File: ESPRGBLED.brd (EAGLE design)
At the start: 160 x 100 mm, 20 parts

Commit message: added layout
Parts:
- removed D4: (no value), diode:SMB
- removed PWR1:R3, PWR2:R3, PWR3:R3: 10k, rcl:R0603
- removed PWR1:R4, PWR2:R4, PWR3:R4: (no value), rcl:R0603
- removed PWR1:T2, PWR2:T2, PWR3:T2: (no value), transistor:SOT23-BEC
- removed SV1: (no value), con-lstb:MA03-1
- added C1, C2: (no value), rcl:C0603K
- added C3, C4: (no value), rcl:C0805K
- added D1: MBRS130LT3, diode:SMB
- added U$3: (no value), Fabian:3-WIRE_CONN
- added U$4, U$5, U$6, U$7, U$8: CON1, Fabian:CON1HP
- PWR1:D1, PWR2:D1, PWR3:D1: value (none) -> MBRS130LT3
- PWR1:T1, PWR2:T1, PWR3:T1: value MOSFET-NIRLR8743 -> (none); device Fabian:DPAK -> zetex:SOT223
- moved U$1 26.7 mm to (128.3, 64.8)
- moved R5 21.9 mm to (127.0, 40.6), turned to 180 degrees
- moved PWR1:D1 19.0 mm to (128.3, 52.7)
- moved PWR2:D1 12.1 mm to (128.3, 48.3)
- moved U$2 9.16 mm to (116.2, 36.2), flipped to the bottom
- moved PWR3:D1 8.28 mm to (128.3, 43.8)
- moved PWR1:T1 5.08 mm to (120.0, 58.4)
- moved PWR3:T1 5.08 mm to (120.0, 43.2)
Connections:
- removed net PWR1:N$4: PWR1:R4.1, PWR1:T2.B
- removed net PWR1:N$5: PWR1:R3.1, PWR1:T1.1, PWR1:T2.C
- removed net PWR1:OUT: PWR1:D1.A, PWR1:T1.4
- removed net PWR2:N$4: PWR2:R4.1, PWR2:T2.B
- removed net PWR2:N$5: PWR2:R3.1, PWR2:T1.1, PWR2:T2.C
- removed net PWR2:OUT: PWR2:D1.A, PWR2:T1.4
- removed net PWR3:N$4: PWR3:R4.1, PWR3:T2.B
- removed net PWR3:N$5: PWR3:R3.1, PWR3:T1.1, PWR3:T2.C
- removed net PWR3:OUT: PWR3:D1.A, PWR3:T1.4
- new net N$1: PWR1:D1.A, PWR1:T1.2, PWR1:T1.4, U$4.P$1
- new net N$4: PWR2:D1.A, PWR2:T1.2, PWR2:T1.4, U$5.P$1
- new net N$5: PWR3:D1.A, PWR3:T1.2, PWR3:T1.4, U$6.P$1
- net +12V: now also C1.1, C3.1, D1.C, U$7.P$1; no longer D4.C, PWR1:R3.2, PWR2:R3.2, PWR3:R3.2
- net GND: now also C1.2, C2.2, C3.2, C4.2, D1.A, U$3.0V, U$8.P$1; no longer D4.A, PWR1:T2.E, PWR2:T2.E, PWR3:T2.E, SV1.1
- net N$2: now also PWR3:T1.1; no longer PWR3:R4.2
- net N$3: now also PWR2:T1.1; no longer PWR2:R4.2
- net N$6: now also PWR1:T1.1; no longer PWR1:R4.2
- net N$7: now also U$3.SIG; no longer SV1.3
- net N$8: now also U$3.5V; no longer SV1.2
- net VCC: now also C2.1, C4.1
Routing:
- net N$6: track 61.2 -> 21.8 mm, vias 0 -> 1
- net +12V: track 67.8 -> 39.9 mm, vias 3 -> 0
- net VCC: track 34.4 -> 54.3 mm, vias 0 -> 2
- net N$11: track 20.1 -> 3.32 mm, vias 0 -> 1
- net N$1: track 0.00 -> 16.4 mm
- net N$4: track 0.00 -> 13.6 mm
- net N$5: track 0.00 -> 12.7 mm
- net N$3: track 23.6 -> 13.1 mm, vias 0 -> 1
- net GND: track 84.8 -> 92.8 mm, vias 3 -> 2
- net PWR2:OUT: track 7.28 -> 0.00 mm
- net PWR1:OUT: track 7.27 -> 0.00 mm
- net PWR3:OUT: track 7.25 -> 0.00 mm
- net PWR2:N$5: track 5.25 -> 0.00 mm
- net PWR1:N$5: track 5.24 -> 0.00 mm
- net PWR3:N$5: track 5.13 -> 0.00 mm
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
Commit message: layouted
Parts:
- added R1: 0R, rcl:R0603
- added U$9: CON1, Fabian:CON1HP
- moved U$7 142.6 mm to (6.35, 3.17), flipped to the bottom, turned to 270 degrees
- moved D1 128.5 mm to (7.62, 3.17), turned to 0 degrees
- moved U$8 121.6 mm to (9.53, 3.17), flipped to the bottom
- moved U$3 121.5 mm to (12.7, 12.1)
- moved U$1 120.3 mm to (16.5, 20.3)
- moved C1 120.0 mm to (18.4, 15.2)
- moved C2 120.0 mm to (14.6, 15.2)
- moved C3 119.8 mm to (18.4, 13.3)
- moved C4 119.8 mm to (14.6, 13.3)
- moved R5 119.3 mm to (8.26, 28.9), turned to 0 degrees
- moved PWR2:D1 118.1 mm to (16.5, 10.2)
- moved PWR3:D1 118.1 mm to (16.5, 5.71)
- moved PWR1:T1 116.9 mm to (8.26, 24.1)
- moved PWR3:T1 116.9 mm to (8.26, 8.89)
- moved PWR2:T1 116.9 mm to (8.26, 16.5)
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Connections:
- new net DGND: C1.2, C2.2, C3.2, C4.2, R1.1, U$1.LEFT, U$2.GND, U$2.GPIO15, U$3.0V
- net +12V: now also U$9.P$1
- net GND: now also R1.2; no longer C1.2, C2.2, C3.2, C4.2, U$1.LEFT, U$2.GND, U$2.GPIO15, U$3.0V
- net N$2: now also U$2.GPIO13
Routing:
- net GND: track 92.8 -> 42.5 mm, vias 2 -> 3
- net DGND: track 0.00 -> 50.1 mm, vias 0 -> 1
- net N$2: track 0.00 -> 28.5 mm, vias 0 -> 1
- net VCC: track 54.3 -> 26.9 mm, vias 2 -> 1
- net +12V: track 39.9 -> 49.0 mm, vias 0 -> 1
- net N$6: track 21.8 -> 15.0 mm
- net N$4: track 13.6 -> 18.8 mm
- net N$3: track 13.1 -> 17.3 mm
- net N$5: track 12.7 -> 15.6 mm
- net N$8: track 13.2 -> 11.2 mm
- net N$7: track 15.1 -> 14.3 mm
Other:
- board size 160 x 100 mm -> 21.3 x 30.1 mm

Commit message: updated layouts
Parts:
- added R2: 0R, rcl:R0603
- moved U$3 6.33 mm to (18.7, 10.2), turned to 90 degrees
- moved R5 3.51 mm to (11.7, 28.6)
- moved D1 2.86 mm to (7.62, 6.03)
- moved PWR3:T1 2.86 mm to (8.26, 11.7)
- moved U$7 2.71 mm to (5.40, 5.71)
- moved U$8 2.62 mm to (8.89, 5.71)
- moved U$9 2.54 mm to (1.91, 5.71)
- moved PWR2:T1 2.22 mm to (8.26, 18.7)
- moved R1 2.22 mm to (12.1, 6.35)
- moved PWR1:T1 1.59 mm to (8.26, 25.7)
- moved U$6 1.59 mm to (1.91, 12.4)
- moved U$4 0.95 mm to (1.91, 27.0)
- moved U$5 0.95 mm to (1.91, 19.4)
- moved PWR3:D1 0.63 mm to (16.5, 6.35)
- moved C1 0.45 mm to (18.1, 15.6)
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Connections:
- new net N$9: R2.1, U$2.GPIO0
- net DGND: now also R2.2
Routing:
- net GND: track 42.5 -> 13.8 mm, vias 3 -> 6
- net N$8: track 11.2 -> 35.7 mm, vias 0 -> 2
- net N$7: track 14.3 -> 33.6 mm, vias 0 -> 2
- net N$2: track 28.5 -> 18.6 mm
- net VCC: track 26.9 -> 35.1 mm
- net N$9: track 0.00 -> 6.03 mm
- net N$4: track 18.8 -> 24.1 mm, vias 0 -> 2
- net N$1: track 16.2 -> 14.1 mm
- net N$11: track 2.97 -> 4.32 mm
- net DGND: track 50.1 -> 48.9 mm, vias 1 -> 2
- net N$5: track 15.6 -> 16.8 mm
- net N$3: track 17.3 -> 16.4 mm
- net +12V: track 49.0 -> 49.6 mm, vias 1 -> 2
- added copper zone on layer 1, net GND
- added copper zone on layer 16, net GND
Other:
- board size 21.3 x 30.1 mm -> 21.3 x 27 mm

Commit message: smd
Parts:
- removed U$2: ESP8266, ESP8266:ESP-03
- added MDL1: (no value), ESP8266-ESP12E:ESP8266-ESP12E
- added R3: 100k, rcl:R0603
- added R4: 10k, rcl:R0603
- R2: device rcl:R0603 -> rcl:R0805
- moved U$8 21.6 mm to (10.5, 27.3)
- moved U$7 21.5 mm to (2.54, 27.0)
- moved U$3 15.6 mm to (18.7, 25.7)
- moved PWR2:D1 12.7 mm to (16.8, 23.2)
- moved R2 10.2 mm to (14.3, 23.8)
- moved R5 6.38 mm to (11.1, 22.2), turned to 270 degrees
- moved C1 4.15 mm to (18.6, 11.4)
- moved C2 4.14 mm to (15.2, 11.4)
- moved C4 4.14 mm to (14.9, 9.53)
- moved C3 4.13 mm to (18.6, 9.53)
- moved U$1 3.97 mm to (16.7, 16.7)
- moved PWR3:D1 1.00 mm to (16.8, 5.40)
- moved R1 0.95 mm to (12.1, 5.40)
- moved U$9 0.71 mm to (2.54, 6.03)
- moved U$4 0.64 mm to (2.54, 27.0)
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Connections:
- new net N$10: MDL1.2, R3.1, R4.2
- net +12V: now also R3.2
- net DGND: now also MDL1.10, MDL1.9; no longer U$2.GND, U$2.GPIO15
- net GND: now also R4.1
- net N$11: now also MDL1.3; no longer U$2.CH_PD
- net N$2: now also MDL1.5; no longer U$2.GPIO13
- net N$3: now also MDL1.6; no longer U$2.GPIO12
- net N$6: now also MDL1.7; no longer U$2.GPIO14
- net N$7: now also MDL1.15; no longer U$2.URXD
- net N$8: now also MDL1.16; no longer U$2.UTXD
- net N$9: now also MDL1.12; no longer U$2.GPIO0
- net VCC: now also MDL1.8; no longer U$2.VCC
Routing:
- net N$10: track 0.00 -> 21.8 mm
- net GND: track 13.8 -> 35.1 mm, vias 6 -> 3
- net N$2: track 18.6 -> 3.10 mm
- net N$4: track 24.1 -> 8.74 mm, vias 2 -> 0
- net N$11: track 4.32 -> 18.0 mm
- net N$6: track 15.3 -> 24.5 mm
- net DGND: track 48.9 -> 40.2 mm, vias 2 -> 1
- net N$9: track 6.03 -> 13.2 mm
- net N$3: track 16.4 -> 9.36 mm
- net +12V: track 49.6 -> 43.7 mm
- net N$8: track 35.7 -> 32.2 mm, vias 2 -> 0
- net N$7: track 33.6 -> 30.3 mm, vias 2 -> 0
- net VCC: track 35.1 -> 32.0 mm
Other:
- board size 21.3 x 27 mm -> 20.3 x 26.3 mm

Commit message: through hole
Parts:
- removed U$4, U$5, U$6, U$7, U$8, U$9: CON1, Fabian:CON1HP
- added LSP1, LSP2, LSP3, LSP4, LSP5, LSP6: LSP10, solpad:LSP10
- moved R4 19.7 mm to (1.91, 5.08), flipped to the top, turned to 180 degrees
- moved R3 17.2 mm to (1.91, 6.67), flipped to the top
- moved PWR1:T1 0.64 mm to (8.26, 25.1)
- moved PWR2:T1 0.64 mm to (8.26, 18.1)
- moved R5 0.64 mm to (11.1, 21.6)
- moved U$3 0.64 mm to (18.7, 25.1)
- moved C1 0.63 mm to (18.6, 10.8)
- moved C2 0.63 mm to (15.2, 10.8)
- moved C3 0.63 mm to (18.6, 8.89)
- moved C4 0.63 mm to (14.9, 8.89)
- moved PWR3:T1 0.63 mm to (8.26, 11.1)
- moved PWR1:D1 0.63 mm to (16.8, 26.7)
- moved PWR2:D1 0.63 mm to (16.8, 22.5)
- moved U$1 0.63 mm to (16.7, 16.0)
- moved MDL1 0.32 mm to (3.49, 20.3)
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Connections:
- net +12V: now also LSP1.MP, LSP5.MP; no longer U$7.P$1, U$9.P$1
- net DGND: now also R4.1
- net GND: now also LSP6.MP; no longer R4.1, U$8.P$1
- net N$1: now also LSP2.MP; no longer U$4.P$1
- net N$4: now also LSP3.MP; no longer U$5.P$1
- net N$5: now also LSP4.MP; no longer U$6.P$1
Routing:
- net DGND: track 40.2 -> 57.0 mm, vias 1 -> 2
- net N$10: track 21.8 -> 5.77 mm, vias 0 -> 1
- net N$3: track 9.36 -> 21.7 mm
- net VCC: track 32.0 -> 40.9 mm
- net GND: track 35.1 -> 42.5 mm, vias 3 -> 14
- net +12V: track 43.7 -> 49.5 mm
- net N$6: track 24.5 -> 18.7 mm
- net N$1: track 13.6 -> 8.66 mm
- net N$8: track 32.2 -> 28.4 mm
- net N$7: track 30.3 -> 27.0 mm, vias 0 -> 2
- net N$4: track 8.74 -> 11.3 mm
- net N$5: track 16.9 -> 17.7 mm
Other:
- board size 20.3 x 26.3 mm -> 22.5 x 25.7 mm

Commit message: minor stuff
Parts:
- moved U$3 0.16 mm to (18.7, 24.9)
- renumbered LSP1 to +, LSP2 to 13, LSP3 to 12, LSP4 to 14, LSP5 to 12V, LSP6 to GND
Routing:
- net N$1: track 8.66 -> 15.1 mm
- net VCC: track 40.9 -> 37.0 mm
- net N$8: track 28.4 -> 27.6 mm, vias 0 -> 2
- net N$7: track 27.0 -> 26.7 mm, vias 2 -> 0
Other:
- board text added: "github.com/fabianhu"

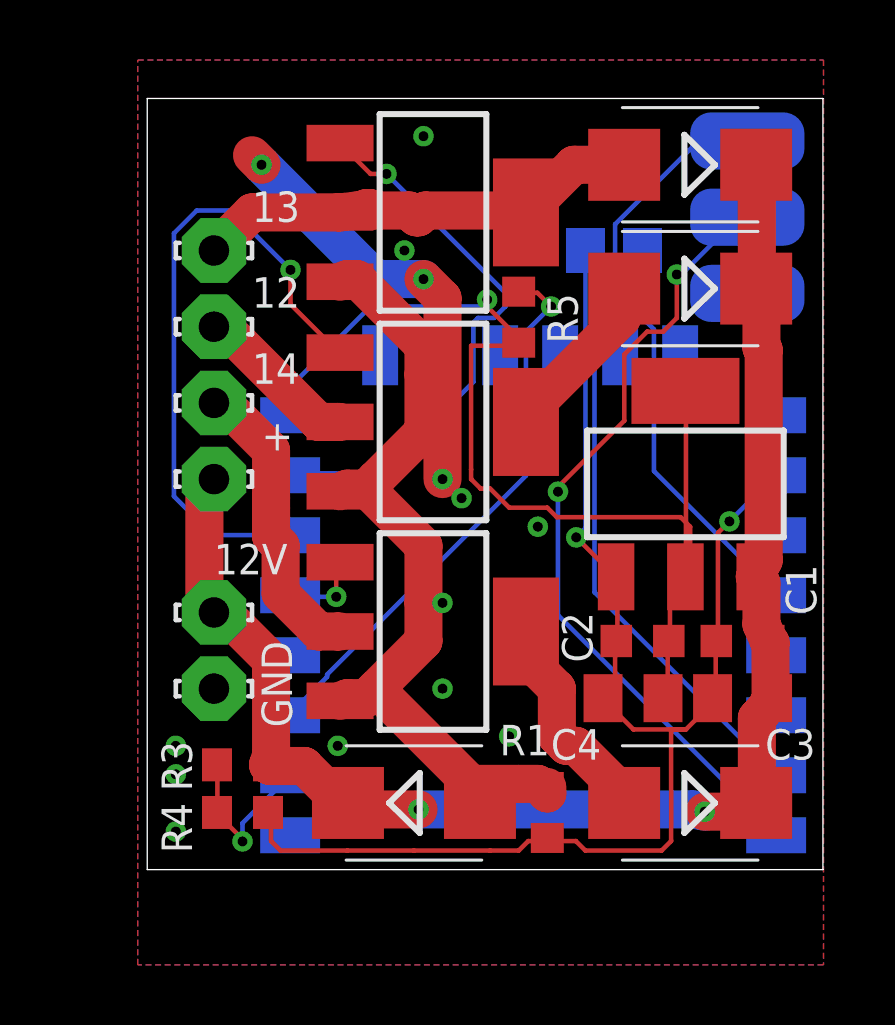
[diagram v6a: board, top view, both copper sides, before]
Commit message: updated HW with reset-wakeup option
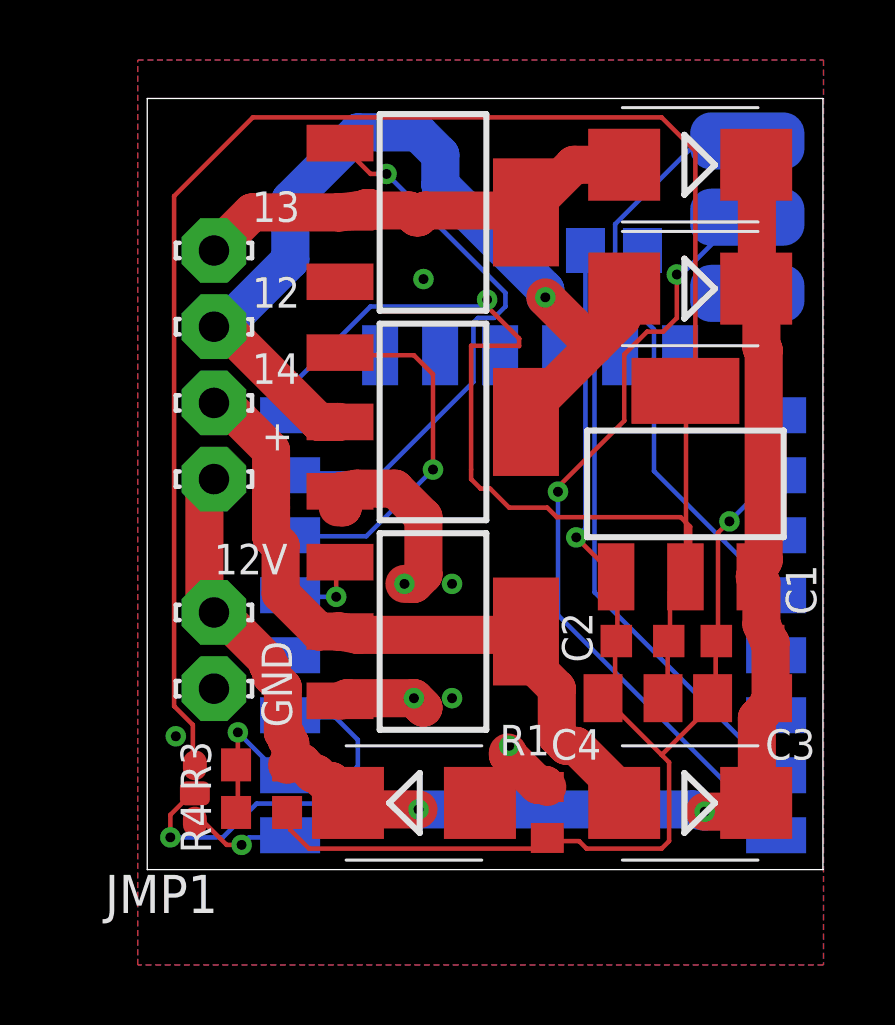
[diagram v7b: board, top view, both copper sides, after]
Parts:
- removed R5: 10k, rcl:R0603
- added JMP1: 0R-JUMPC, jump-0r-smd:C0R-JMP
- moved R3 0.64 mm to (2.54, 6.67)
- moved R4 0.64 mm to (2.54, 5.08)
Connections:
- new net N$12: JMP1.2, MDL1.3
- net N$11: now also JMP1.1, MDL1.1; no longer MDL1.3, R5.1
- net VCC: now also JMP1.3; no longer R5.2
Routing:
- net VCC: track 37.0 -> 83.4 mm
- net GND: track 42.5 -> 11.8 mm, vias 14 -> 7
- net N$4: track 11.3 -> 31.6 mm, vias 0 -> 1
- net N$11: track 18.5 -> 3.61 mm
- net N$12: track 0.00 -> 12.6 mm, vias 0 -> 1
- net N$3: track 21.7 -> 12.3 mm
- net N$5: track 17.7 -> 23.9 mm
- net DGND: track 57.1 -> 55.5 mm
- net N$10: track 5.77 -> 5.07 mm
